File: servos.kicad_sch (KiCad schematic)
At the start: 5 parts, among them J10 Conn_01x03_Pin, J11 Conn_01x03_Pin, J12 Conn_01x03_Pin, Q1 IPD90N04S4-05, SW2 PTS 647 SN50 SMTR2 LFS

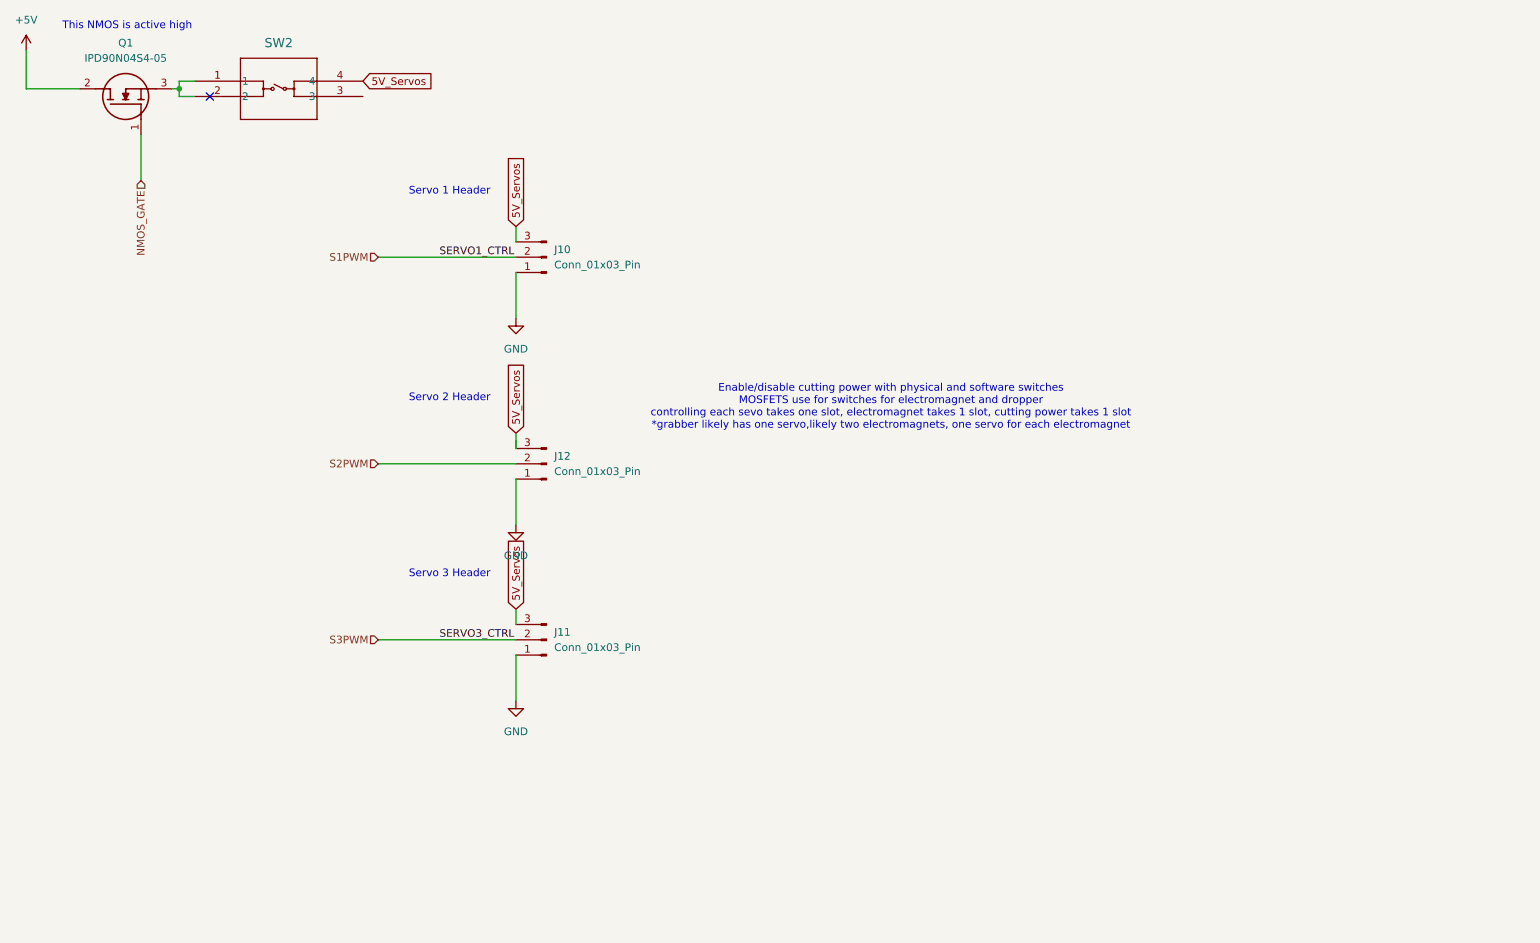
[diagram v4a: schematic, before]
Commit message: added updated pinouts for grabber servo and dropper emagnets
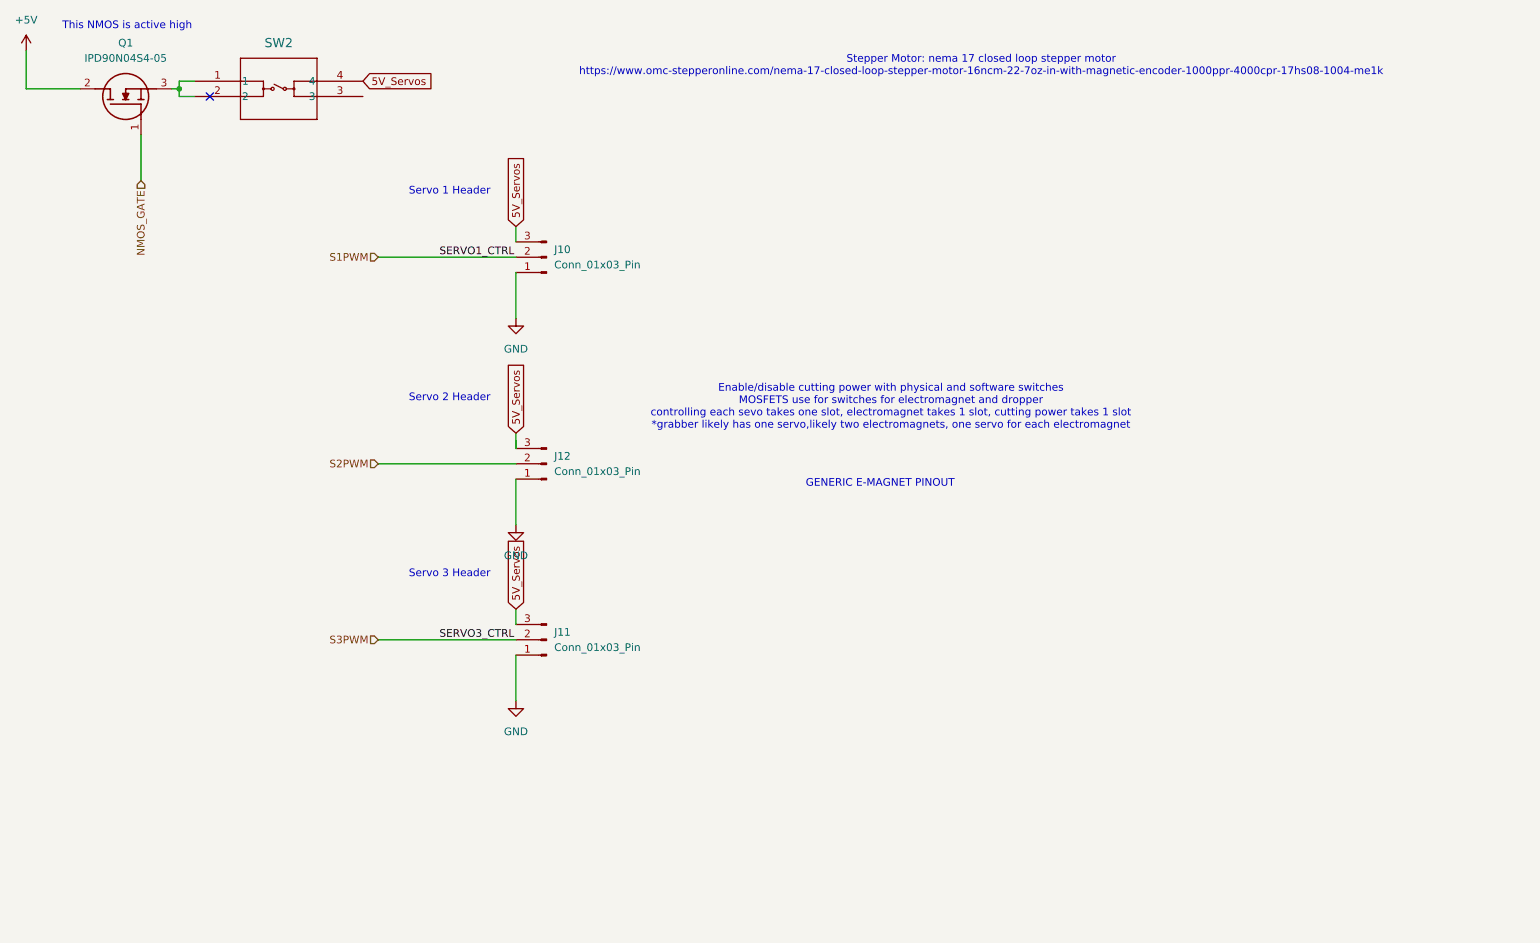
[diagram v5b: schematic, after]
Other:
- note added: "GENERIC E-MAGNET PINOUT"
- note added: "Stepper Motor: nema 17 closed loop stepper motor https://www.omc-stepperonline.com/nema-17-closed-loop-stepper-motor-16ncm-22-7oz-in-with-magnetic-encoder-1000ppr-4000cpr-17hs08-1004-me1k"

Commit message: updated servos with new connectors
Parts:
- removed J10, J11, J12: Conn_01x03_Pin, Connector_PinHeader_2.54mm:PinHeader_1x03_P2.54mm_Vertical, symbol Connector:Conn_01x03_Pin
- added J10, J9: Conn_01x02_Pin, symbol Connector:Conn_01x02_Pin
- added J7: Conn_01x04, symbol Connector_Generic:Conn_01x04
- added J8: Conn_02x04_Counter_Clockwise, symbol Connector_Generic:Conn_02x04_Counter_Clockwise
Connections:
- net 5V_Servos: now also J10.2 (Pin_2), J7.1 (Pin_1), J7.3 (Pin_3), J8.1 (Pin_1), J9.2 (Pin_2)
- net GND: now also J10.1 (Pin_1), J7.2 (Pin_2), J7.4 (Pin_4), J8.2 (Pin_2), J9.1 (Pin_1)
- new net EA+: J8.3 (Pin_3)
- new net EA-: J8.4 (Pin_4)
- new net EB+: J8.8 (Pin_8)
- new net EB-: J8.7 (Pin_7)
- new net EZ+: J8.6 (Pin_6)
- new net EZ-: J8.5 (Pin_5)
- no-connect marks 1 -> 7

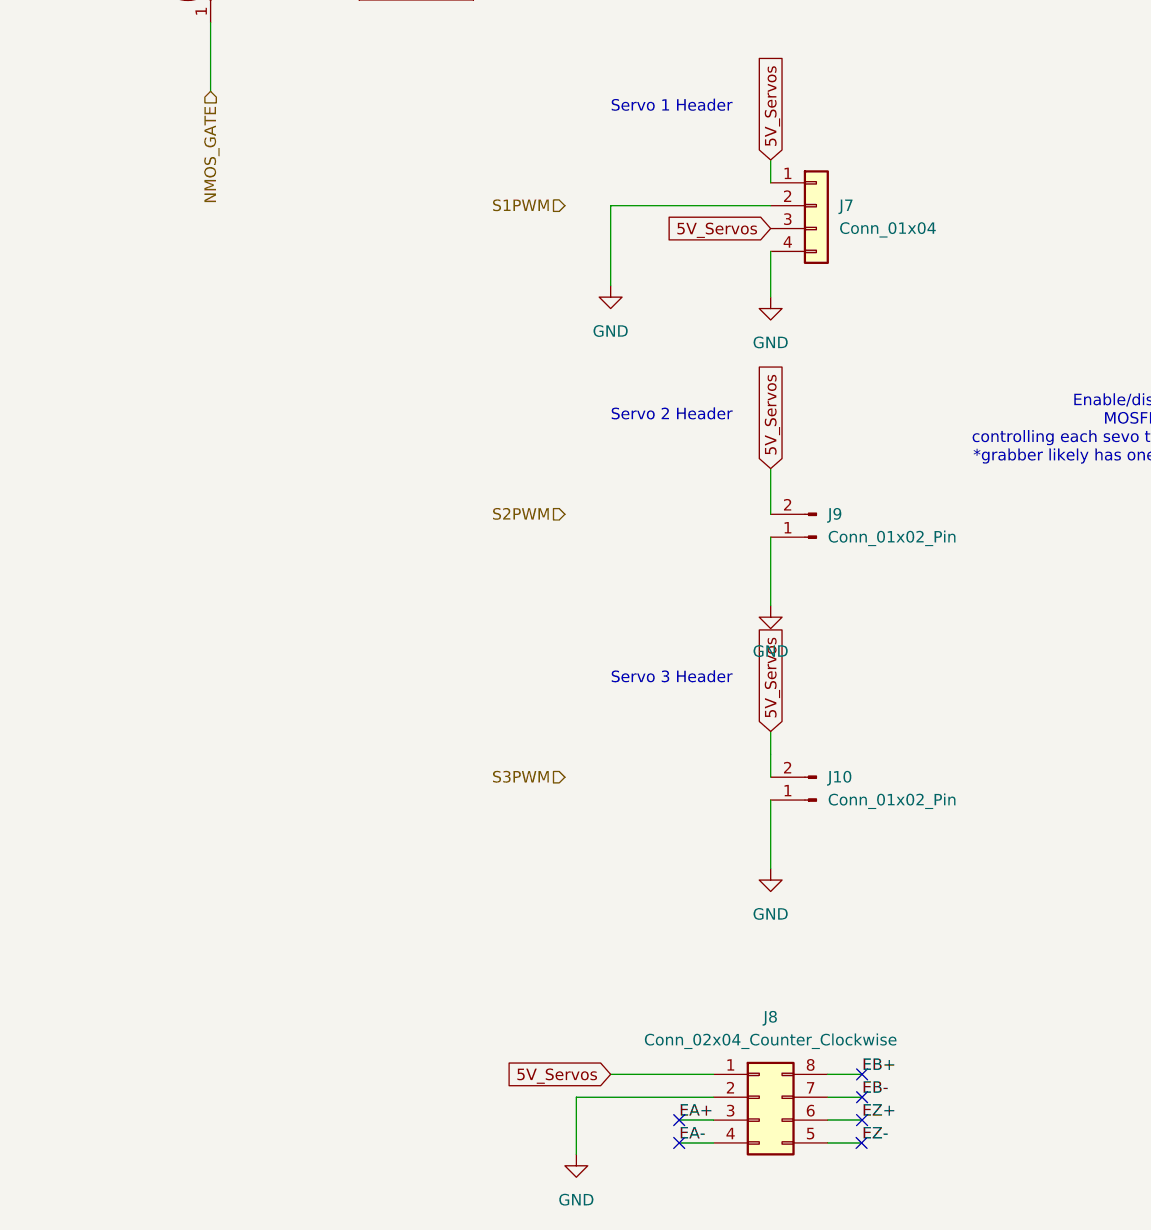
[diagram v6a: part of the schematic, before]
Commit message: updated servos page with em connections
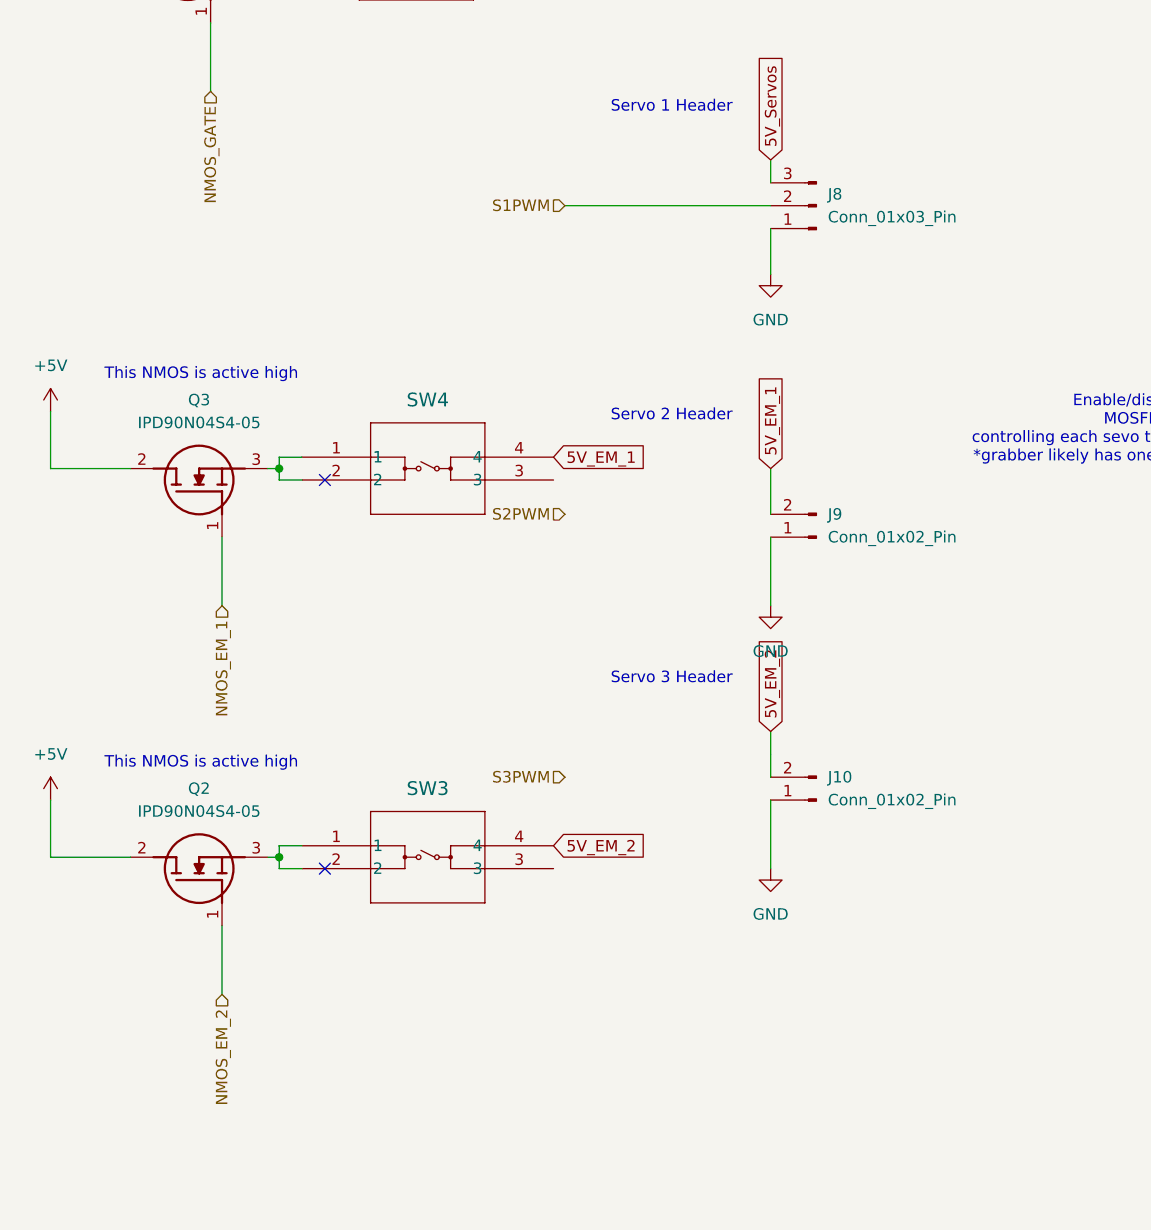
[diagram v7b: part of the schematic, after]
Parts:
- removed J7: Conn_01x04, symbol Connector_Generic:Conn_01x04
- removed J8: Conn_02x04_Counter_Clockwise, symbol Connector_Generic:Conn_02x04_Counter_Clockwise
- added J8: Conn_01x03_Pin, symbol Connector:Conn_01x03_Pin
- added Q2, Q3: IPD90N04S4-05, IPD90N04S405, symbol AquaPartsLib:IPD90N04S4-05
- added SW3, SW4: PTS 647 SN50 SMTR2 LFS, AquaPartsLib:SW_PTS_647_SN50_SMTR2_LFS, symbol AquaPartsLib:PTS_647_SN50_SMTR2_LFS
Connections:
- net +5V: now also Q2.2 (D), Q3.2 (D)
- net 5V_Servos: now also J8.3 (Pin_3); no longer J10.2 (Pin_2), J9.2 (Pin_2)
- net GND: now also J8.1 (Pin_1)
- net S1PWM: now also J8.2 (Pin_2)
- new net: Q2.3 (S), SW3.1, SW3.2
- new net: Q3.3 (S), SW4.1, SW4.2
- new net 5V_EM_1: J9.2 (Pin_2), SW4.4
- new net 5V_EM_2: J10.2 (Pin_2), SW3.4
- new net NMOS_EM_1: Q3.1 (G)
- new net NMOS_EM_2: Q2.1 (G)
- no-connect marks 7 -> 3
